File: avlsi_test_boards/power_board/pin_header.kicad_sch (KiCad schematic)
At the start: 3 parts, among them J5 Conn_01x02_Pin, J6 Conn_01x02_Pin

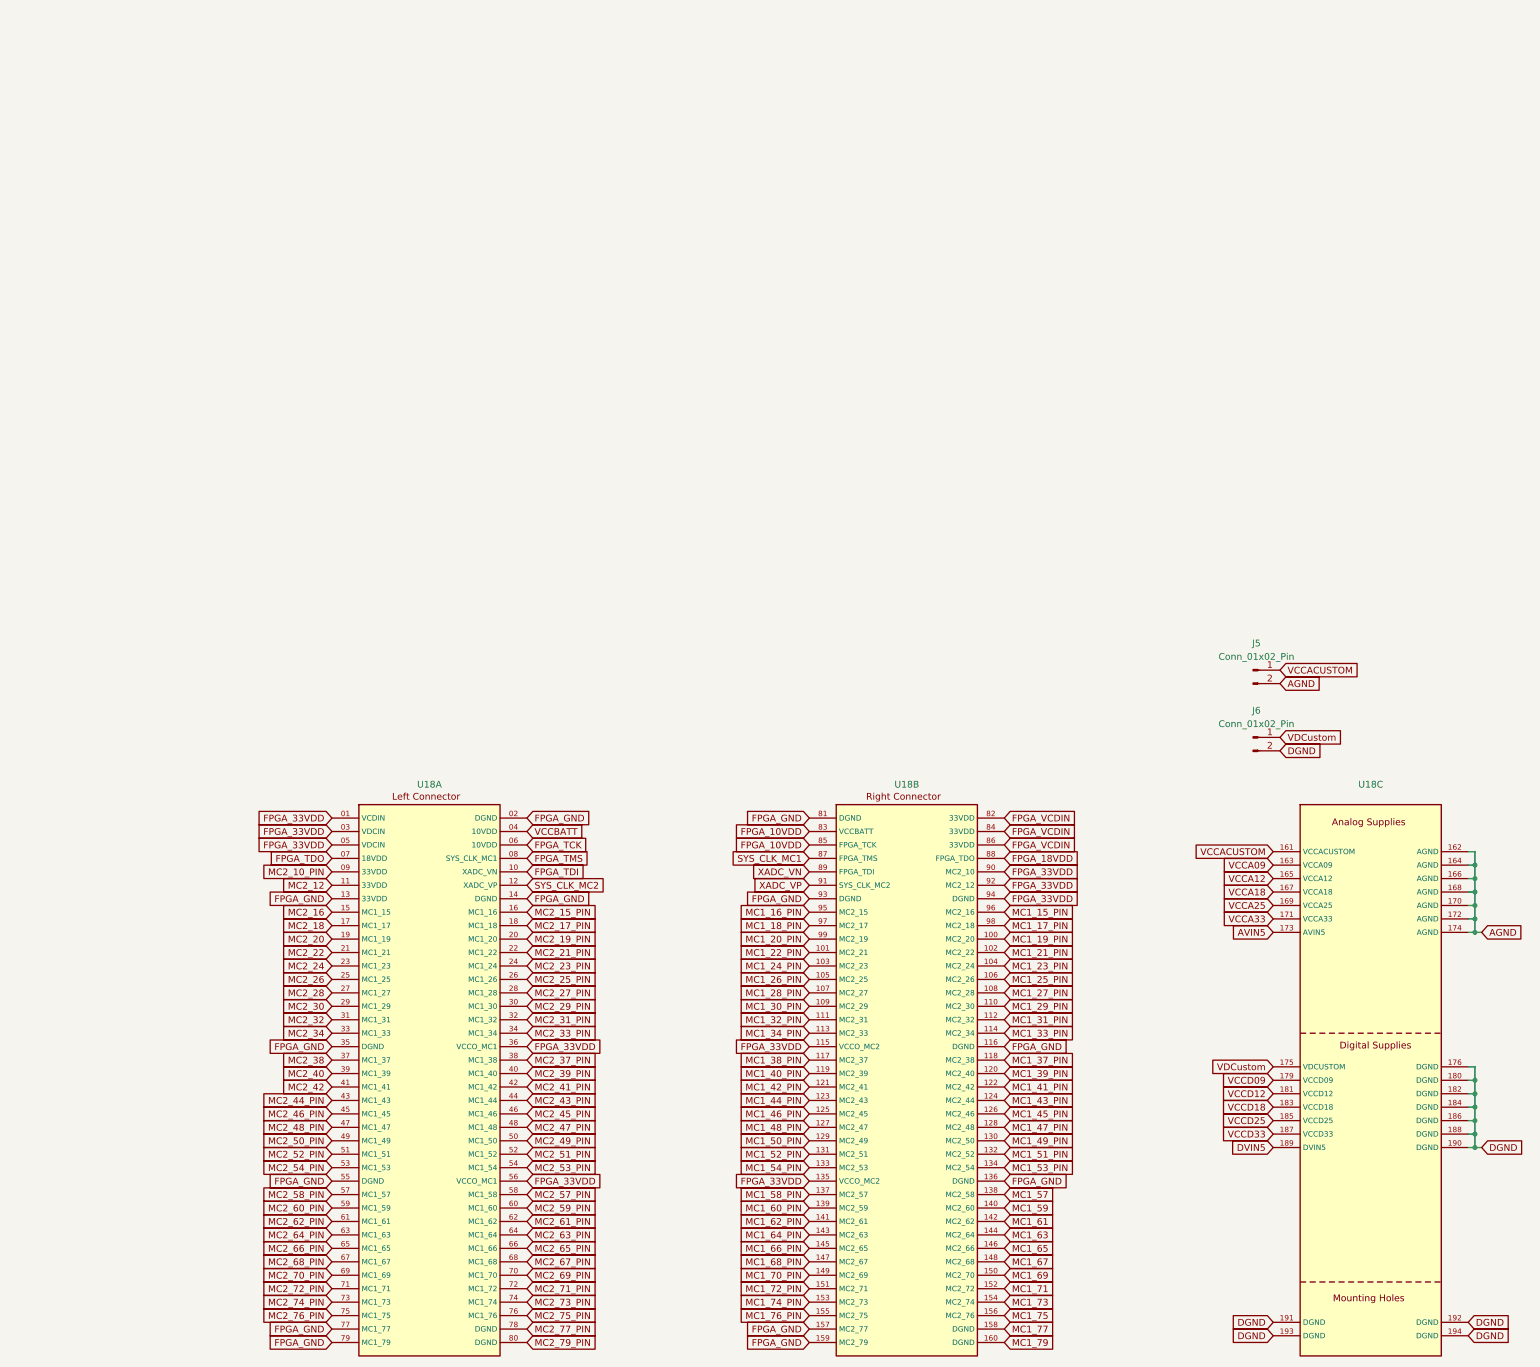
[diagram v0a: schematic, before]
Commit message: Add updated power board layout and schematic
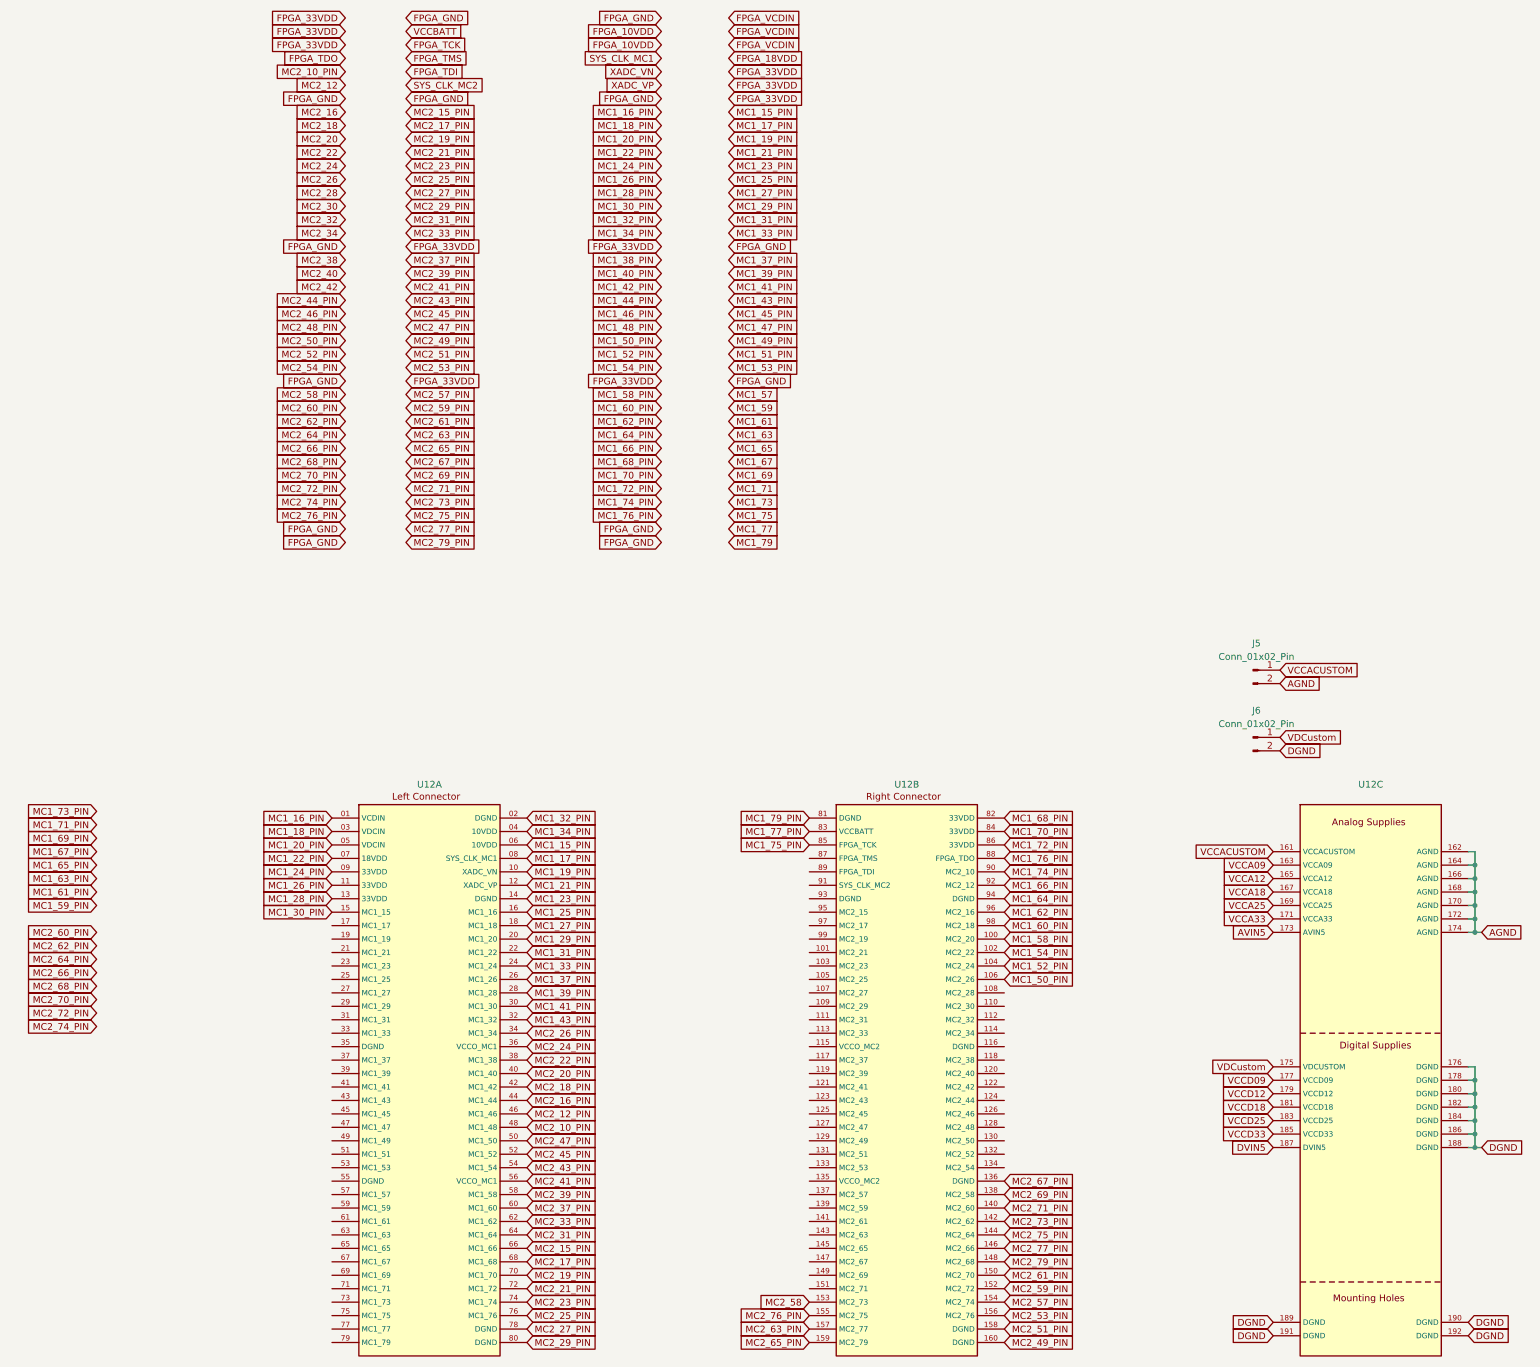
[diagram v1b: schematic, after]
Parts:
- renumbered U18 to U12
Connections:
- net DGND: now also U12.178 (DGND), U12.189 (DGND); no longer U12.193 (DGND), U12.194 (DGND)
- net DVIN5: now also U12.187 (DVIN5); no longer U12.189 (DVIN5)
- net FPGA_10VDD: no longer U12.83 (VCCBATT), U12.85 (FPGA_TCK)
- net FPGA_18VDD: no longer U12.88 (FPGA_TDO)
- net FPGA_33VDD: no longer U12.01 (VCDIN), U12.03 (VDCIN), U12.05 (VDCIN), U12.115 (VCCO_MC2), U12.135 (VCCO_MC2), U12.36 (VCCO_MC1), U12.56 (VCCO_MC1), U12.90 (MC2_10), U12.92 (MC2_12), U12.94 (DGND)
- net FPGA_GND: no longer U12.02 (DGND), U12.116 (DGND), U12.13 (33VDD), U12.136 (DGND), U12.14 (DGND), U12.157 (MC2_77), U12.159 (MC2_79), U12.35 (DGND), U12.55 (DGND), U12.77 (MC1_77), U12.79 (MC1_79), U12.81 (DGND), U12.93 (DGND)
- net FPGA_TCK: no longer U12.06 (10VDD)
- net FPGA_TDI: no longer U12.10 (XADC_VN)
- net FPGA_TDO: no longer U12.07 (18VDD)
- net FPGA_TMS: no longer U12.08 (SYS_CLK_MC1)
- net FPGA_VCDIN: no longer U12.82 (33VDD), U12.84 (33VDD), U12.86 (33VDD)
- net MC1_15_PIN: now also U12.06 (10VDD); no longer U12.96 (MC2_16)
- net MC1_16_PIN: now also U12.01 (VCDIN); no longer U12.95 (MC2_15)
- net MC1_17_PIN: now also U12.08 (SYS_CLK_MC1); no longer U12.98 (MC2_18)
- net MC1_18_PIN: now also U12.03 (VDCIN); no longer U12.97 (MC2_17)
- net MC1_19_PIN: now also U12.10 (XADC_VN); no longer U12.100 (MC2_20)
- net MC1_20_PIN: now also U12.05 (VDCIN); no longer U12.99 (MC2_19)
- net MC1_21_PIN: now also U12.12 (XADC_VP); no longer U12.102 (MC2_22)
- net MC1_22_PIN: now also U12.07 (18VDD); no longer U12.101 (MC2_21)
- net MC1_23_PIN: now also U12.14 (DGND); no longer U12.104 (MC2_24)
- net MC1_24_PIN: now also U12.09 (33VDD); no longer U12.103 (MC2_23)
- net MC1_25_PIN: now also U12.16 (MC1_16); no longer U12.106 (MC2_26)
- net MC1_26_PIN: now also U12.11 (33VDD); no longer U12.105 (MC2_25)
- net MC1_27_PIN: now also U12.18 (MC1_18); no longer U12.108 (MC2_28)
- net MC1_28_PIN: now also U12.13 (33VDD); no longer U12.107 (MC2_27)
- net MC1_29_PIN: now also U12.20 (MC1_20); no longer U12.110 (MC2_30)
- net MC1_30_PIN: now also U12.15 (MC1_15); no longer U12.109 (MC2_29)
- net MC1_31_PIN: now also U12.22 (MC1_22); no longer U12.112 (MC2_32)
- net MC1_32_PIN: now also U12.02 (DGND); no longer U12.111 (MC2_31)
- net MC1_33_PIN: now also U12.24 (MC1_24); no longer U12.114 (MC2_34)
- net MC1_34_PIN: now also U12.04 (10VDD); no longer U12.113 (MC2_33)
- net MC1_37_PIN: now also U12.26 (MC1_26); no longer U12.118 (MC2_38)
- net MC1_38_PIN: no longer U12.117 (MC2_37)
- net MC1_39_PIN: now also U12.28 (MC1_28); no longer U12.120 (MC2_40)
- net MC1_40_PIN: no longer U12.119 (MC2_39)
- net MC1_41_PIN: now also U12.30 (MC1_30); no longer U12.122 (MC2_42)
- net MC1_42_PIN: no longer U12.121 (MC2_41)
- net MC1_43_PIN: now also U12.32 (MC1_32); no longer U12.124 (MC2_44)
- net MC1_44_PIN: no longer U12.123 (MC2_43)
- net MC1_45_PIN: no longer U12.126 (MC2_46)
- net MC1_46_PIN: no longer U12.125 (MC2_45)
- net MC1_47_PIN: no longer U12.128 (MC2_48)
- net MC1_48_PIN: no longer U12.127 (MC2_47)
- net MC1_49_PIN: no longer U12.130 (MC2_50)
- net MC1_50_PIN: now also U12.106 (MC2_26); no longer U12.129 (MC2_49)
- net MC1_51_PIN: no longer U12.132 (MC2_52)
- net MC1_52_PIN: now also U12.104 (MC2_24); no longer U12.131 (MC2_51)
- net MC1_53_PIN: no longer U12.134 (MC2_54)
- net MC1_54_PIN: now also U12.102 (MC2_22); no longer U12.133 (MC2_53)
- net MC1_57: no longer U12.138 (MC2_58)
- net MC1_58_PIN: now also U12.100 (MC2_20); no longer U12.137 (MC2_57)
- net MC1_59: no longer U12.140 (MC2_60)
- net MC1_60_PIN: now also U12.98 (MC2_18); no longer U12.139 (MC2_59)
- net MC1_61: no longer U12.142 (MC2_62)
- net MC1_62_PIN: now also U12.96 (MC2_16); no longer U12.141 (MC2_61)
- net MC1_63: no longer U12.144 (MC2_64)
- net MC1_64_PIN: now also U12.94 (DGND); no longer U12.143 (MC2_63)
- net MC1_65: no longer U12.146 (MC2_66)
- net MC1_66_PIN: now also U12.92 (MC2_12); no longer U12.145 (MC2_65)
- net MC1_67: no longer U12.148 (MC2_68)
- net MC1_68_PIN: now also U12.82 (33VDD); no longer U12.147 (MC2_67)
- net MC1_69: no longer U12.150 (MC2_70)
- net MC1_70_PIN: now also U12.84 (33VDD); no longer U12.149 (MC2_69)
- net MC1_71: no longer U12.152 (MC2_72)
- net MC1_72_PIN: now also U12.86 (33VDD); no longer U12.151 (MC2_71)
- net MC1_73: no longer U12.154 (MC2_74)
- net MC1_74_PIN: now also U12.90 (MC2_10); no longer U12.153 (MC2_73)
- net MC1_75: no longer U12.156 (MC2_76)
- net MC1_76_PIN: now also U12.88 (FPGA_TDO); no longer U12.155 (MC2_75)
- net MC1_77: no longer U12.158 (DGND)
- net MC1_79: no longer U12.160 (DGND)
- net MC2_10_PIN: now also U12.48 (MC1_48); no longer U12.09 (33VDD)
- net MC2_12: no longer U12.11 (33VDD)
- net MC2_15_PIN: now also U12.66 (MC1_66); no longer U12.16 (MC1_16)
- net MC2_16: no longer U12.15 (MC1_15)
- net MC2_17_PIN: now also U12.68 (MC1_68); no longer U12.18 (MC1_18)
- net MC2_18: no longer U12.17 (MC1_17)
- net MC2_19_PIN: now also U12.70 (MC1_70); no longer U12.20 (MC1_20)
- net MC2_20: no longer U12.19 (MC1_19)
- net MC2_21_PIN: now also U12.72 (MC1_72); no longer U12.22 (MC1_22)
- net MC2_22: no longer U12.21 (MC1_21)
- net MC2_23_PIN: now also U12.74 (MC1_74); no longer U12.24 (MC1_24)
- net MC2_24: no longer U12.23 (MC1_23)
- net MC2_25_PIN: now also U12.76 (MC1_76); no longer U12.26 (MC1_26)
- net MC2_26: no longer U12.25 (MC1_25)
- net MC2_27_PIN: now also U12.78 (DGND); no longer U12.28 (MC1_28)
- net MC2_28: no longer U12.27 (MC1_27)
- net MC2_29_PIN: now also U12.80 (DGND); no longer U12.30 (MC1_30)
- net MC2_30: no longer U12.29 (MC1_29)
- net MC2_31_PIN: now also U12.64 (MC1_64); no longer U12.32 (MC1_32)
- net MC2_32: no longer U12.31 (MC1_31)
- net MC2_33_PIN: now also U12.62 (MC1_62); no longer U12.34 (MC1_34)
- net MC2_34: no longer U12.33 (MC1_33)
- net MC2_37_PIN: now also U12.60 (MC1_60); no longer U12.38 (MC1_38)
- net MC2_38: no longer U12.37 (MC1_37)
- net MC2_39_PIN: now also U12.58 (MC1_58); no longer U12.40 (MC1_40)
- net MC2_40: no longer U12.39 (MC1_39)
- net MC2_41_PIN: now also U12.56 (VCCO_MC1); no longer U12.42 (MC1_42)
- net MC2_42: no longer U12.41 (MC1_41)
- net MC2_43_PIN: now also U12.54 (MC1_54); no longer U12.44 (MC1_44)
- net MC2_44_PIN: no longer U12.43 (MC1_43)
- net MC2_45_PIN: now also U12.52 (MC1_52); no longer U12.46 (MC1_46)
- net MC2_46_PIN: no longer U12.45 (MC1_45)
- net MC2_47_PIN: now also U12.50 (MC1_50); no longer U12.48 (MC1_48)
- net MC2_48_PIN: no longer U12.47 (MC1_47)
- net MC2_49_PIN: now also U12.160 (DGND); no longer U12.50 (MC1_50)
- net MC2_50_PIN: no longer U12.49 (MC1_49)
- net MC2_51_PIN: now also U12.158 (DGND); no longer U12.52 (MC1_52)
- net MC2_52_PIN: no longer U12.51 (MC1_51)
- net MC2_53_PIN: now also U12.156 (MC2_76); no longer U12.54 (MC1_54)
- net MC2_54_PIN: no longer U12.53 (MC1_53)
- net MC2_57_PIN: now also U12.154 (MC2_74); no longer U12.58 (MC1_58)
- net MC2_58_PIN: no longer U12.57 (MC1_57)
- net MC2_59_PIN: now also U12.152 (MC2_72); no longer U12.60 (MC1_60)
- net MC2_60_PIN: no longer U12.59 (MC1_59)
- net MC2_61_PIN: now also U12.150 (MC2_70); no longer U12.62 (MC1_62)
- net MC2_62_PIN: no longer U12.61 (MC1_61)
- net MC2_63_PIN: now also U12.157 (MC2_77); no longer U12.64 (MC1_64)
- net MC2_64_PIN: no longer U12.63 (MC1_63)
- net MC2_65_PIN: now also U12.159 (MC2_79); no longer U12.66 (MC1_66)
- net MC2_66_PIN: no longer U12.65 (MC1_65)
- net MC2_67_PIN: now also U12.136 (DGND); no longer U12.68 (MC1_68)
- net MC2_68_PIN: no longer U12.67 (MC1_67)
- net MC2_69_PIN: now also U12.138 (MC2_58); no longer U12.70 (MC1_70)
- net MC2_70_PIN: no longer U12.69 (MC1_69)
- net MC2_71_PIN: now also U12.140 (MC2_60); no longer U12.72 (MC1_72)
- net MC2_72_PIN: no longer U12.71 (MC1_71)
- net MC2_73_PIN: now also U12.142 (MC2_62); no longer U12.74 (MC1_74)
- net MC2_74_PIN: no longer U12.73 (MC1_73)
- net MC2_75_PIN: now also U12.144 (MC2_64); no longer U12.76 (MC1_76)
- net MC2_76_PIN: now also U12.155 (MC2_75); no longer U12.75 (MC1_75)
- net MC2_77_PIN: now also U12.146 (MC2_66); no longer U12.78 (DGND)
- net MC2_79_PIN: now also U12.148 (MC2_68); no longer U12.80 (DGND)
- net SYS_CLK_MC1: no longer U12.87 (FPGA_TMS)
- net SYS_CLK_MC2: no longer U12.12 (XADC_VP)
- net VCCBATT: no longer U12.04 (10VDD)
- net VCCD09: now also U12.177 (VCCD09); no longer U12.179 (VCCD09)
- net VCCD12: now also U12.179 (VCCD12); no longer U12.181 (VCCD12)
- net VCCD18: now also U12.181 (VCCD18); no longer U12.183 (VCCD18)
- net VCCD25: now also U12.183 (VCCD25); no longer U12.185 (VCCD25)
- net VCCD33: now also U12.185 (VCCD33); no longer U12.187 (VCCD33)
- net XADC_VN: no longer U12.89 (FPGA_TDI)
- net XADC_VP: no longer U12.91 (SYS_CLK_MC2)
- new net MC1_75_PIN: U12.85 (FPGA_TCK)
- new net MC1_77_PIN: U12.83 (VCCBATT)
- new net MC1_79_PIN: U12.81 (DGND)
- new net MC2_12_PIN: U12.46 (MC1_46)
- new net MC2_16_PIN: U12.44 (MC1_44)
- new net MC2_18_PIN: U12.42 (MC1_42)
- new net MC2_20_PIN: U12.40 (MC1_40)
- new net MC2_22_PIN: U12.38 (MC1_38)
- new net MC2_24_PIN: U12.36 (VCCO_MC1)
- new net MC2_26_PIN: U12.34 (MC1_34)
- new net MC2_58: U12.153 (MC2_73)

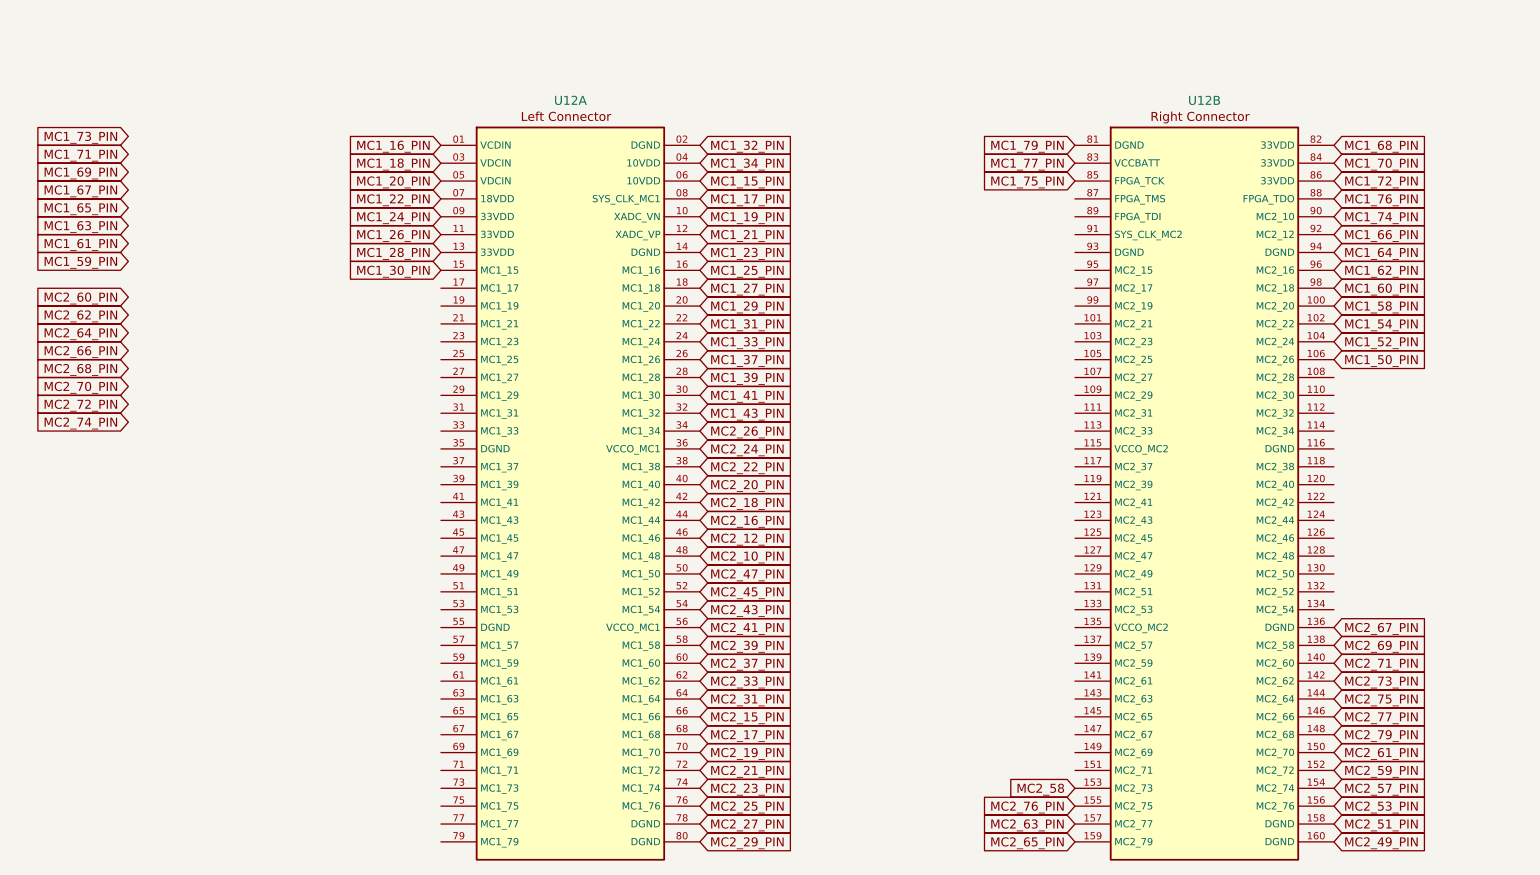
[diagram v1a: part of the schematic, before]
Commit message: Add updated power board
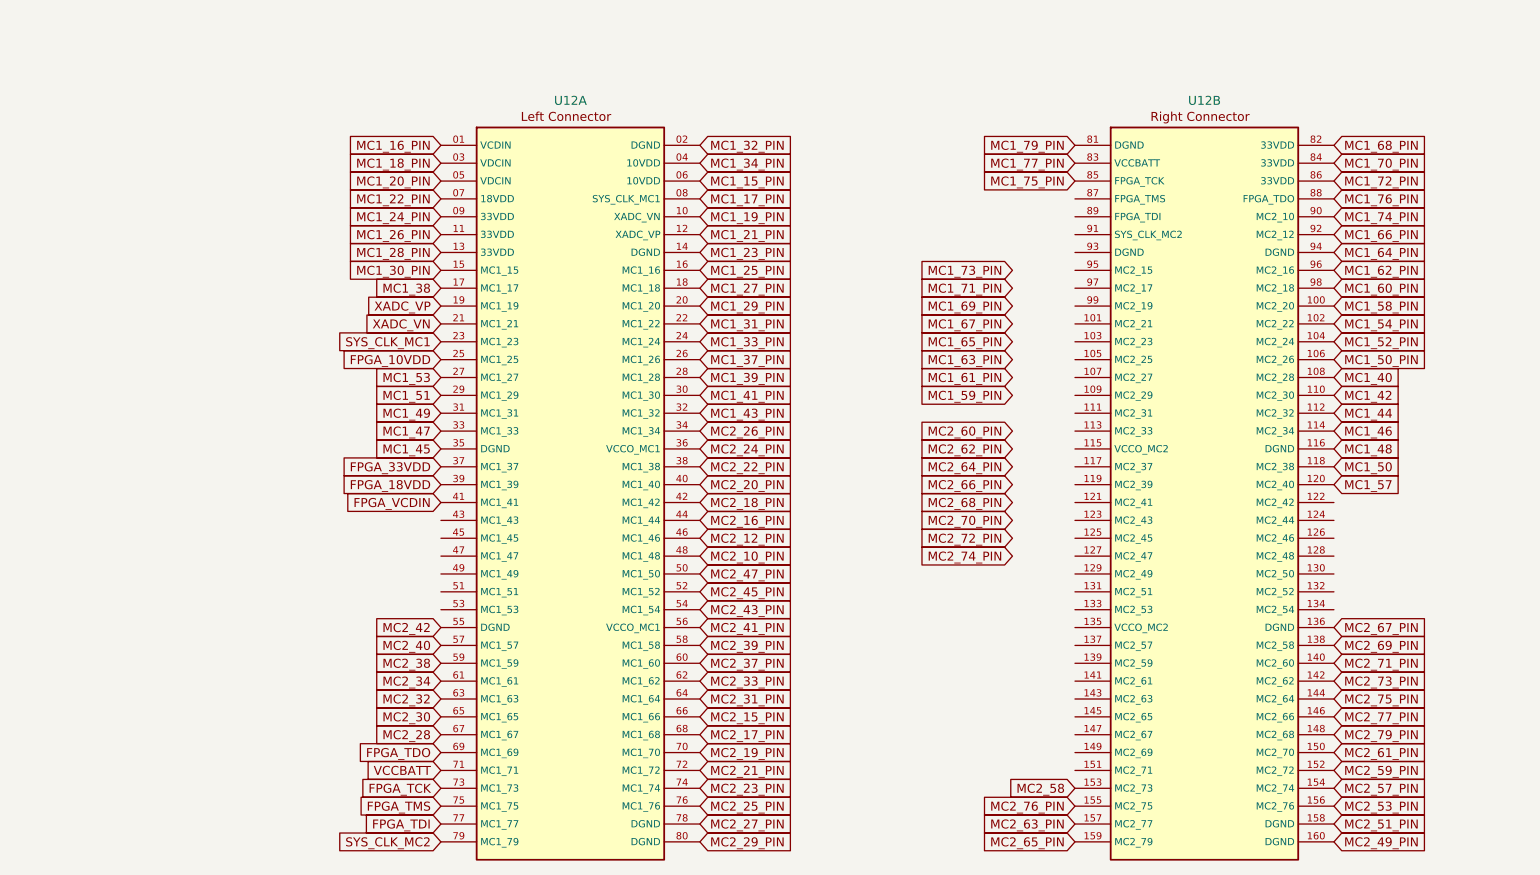
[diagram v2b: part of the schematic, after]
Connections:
- net FPGA_10VDD: now also U12.25 (MC1_25)
- net FPGA_18VDD: now also U12.39 (MC1_39)
- net FPGA_33VDD: now also U12.37 (MC1_37)
- net FPGA_TCK: now also U12.73 (MC1_73)
- net FPGA_TDI: now also U12.77 (MC1_77)
- net FPGA_TDO: now also U12.69 (MC1_69)
- net FPGA_TMS: now also U12.75 (MC1_75)
- net FPGA_VCDIN: now also U12.41 (MC1_41)
- net MC1_57: now also U12.120 (MC2_40)
- net MC2_28: now also U12.67 (MC1_67)
- net MC2_30: now also U12.65 (MC1_65)
- net MC2_32: now also U12.63 (MC1_63)
- net MC2_34: now also U12.61 (MC1_61)
- net MC2_38: now also U12.59 (MC1_59)
- net MC2_40: now also U12.57 (MC1_57)
- net MC2_42: now also U12.55 (DGND)
- net SYS_CLK_MC1: now also U12.23 (MC1_23)
- net SYS_CLK_MC2: now also U12.79 (MC1_79)
- net VCCBATT: now also U12.71 (MC1_71)
- net XADC_VN: now also U12.21 (MC1_21)
- net XADC_VP: now also U12.19 (MC1_19)
- net MC1_40: now reaches U12.108 (MC2_28)
- net MC1_42: now reaches U12.110 (MC2_30)
- net MC1_44: now reaches U12.112 (MC2_32)
- net MC1_46: now reaches U12.114 (MC2_34)
- net MC1_48: now reaches U12.116 (DGND)
- net MC1_50: now reaches U12.118 (MC2_38)
- net MC1_38: now reaches U12.17 (MC1_17)
- net MC1_53: now reaches U12.27 (MC1_27)
- net MC1_51: now reaches U12.29 (MC1_29)
- net MC1_49: now reaches U12.31 (MC1_31)
- net MC1_47: now reaches U12.33 (MC1_33)
- net MC1_45: now reaches U12.35 (DGND)
